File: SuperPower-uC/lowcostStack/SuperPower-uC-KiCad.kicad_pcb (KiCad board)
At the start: 4 copper layers, 92.2 x 45.2 mm, 104 parts, among them J1 Battery connector, J10 External NTC, J11 DNP, J2 Thermistor, J3 USB_B_Micro, J4 Solar in, J5 Conn_01x14_Female, J6 Conn_01x14_Female, J7 DNP, J8 regulator board, J9 MCU board, Q1 2N7002, Q2 2N7002, Q3 S8050, Q4 S8050, Q5 AO3401A, Q6 AO3401A, Q7 2N7002, Q8 2N7002, Q9 AO3401A, SW1 DNP, SW2 DNP, U1 AP9101CK6-ADTRG1, U10 FP6291LR, U11 ME6210A33P, U12 ME6210A33P, U13 ESP32-WROOM32, U14 W25Q32JVSS, U2 FS8205A, U3 LC709203FQH, U4 TP4056, U5 CH340G, U6 AMS1117-3.3, U7 PCF8563T, U8 XC6206P332MR, U9 TCA6408A, Y1 12MHZ, Y2 32.768KHz

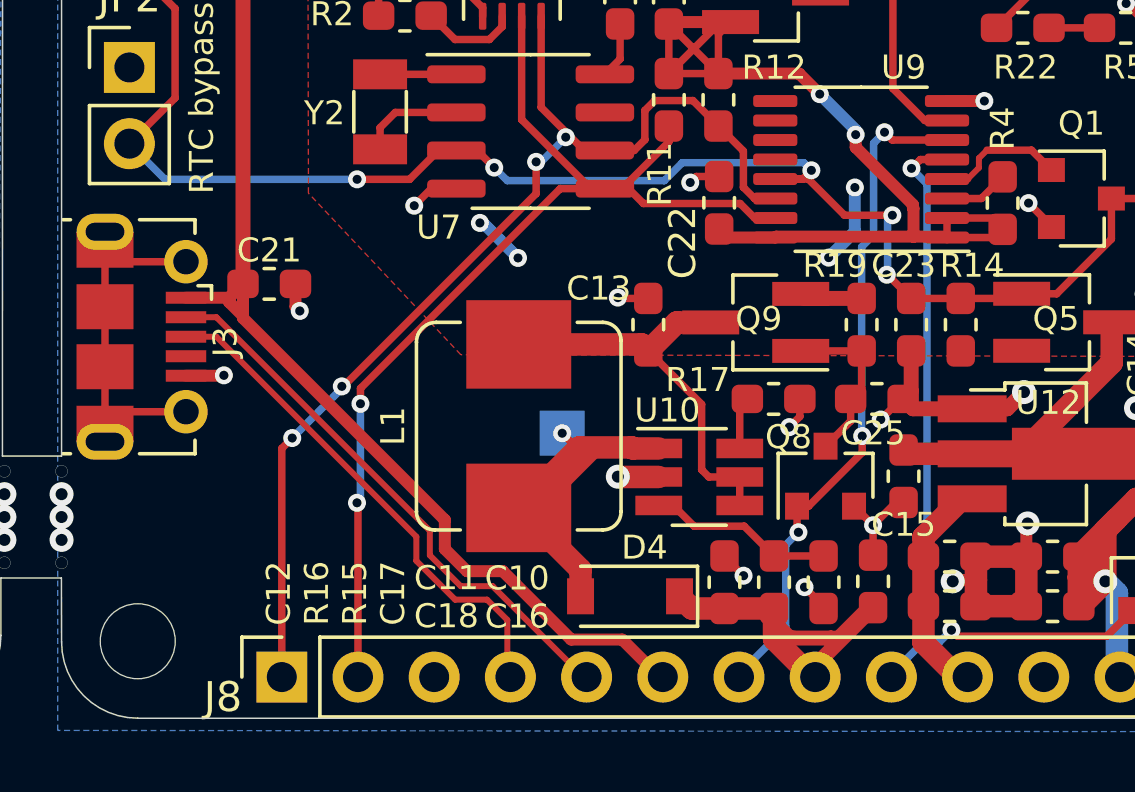
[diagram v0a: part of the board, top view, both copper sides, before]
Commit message: swapped tracks of boost conveter for planes
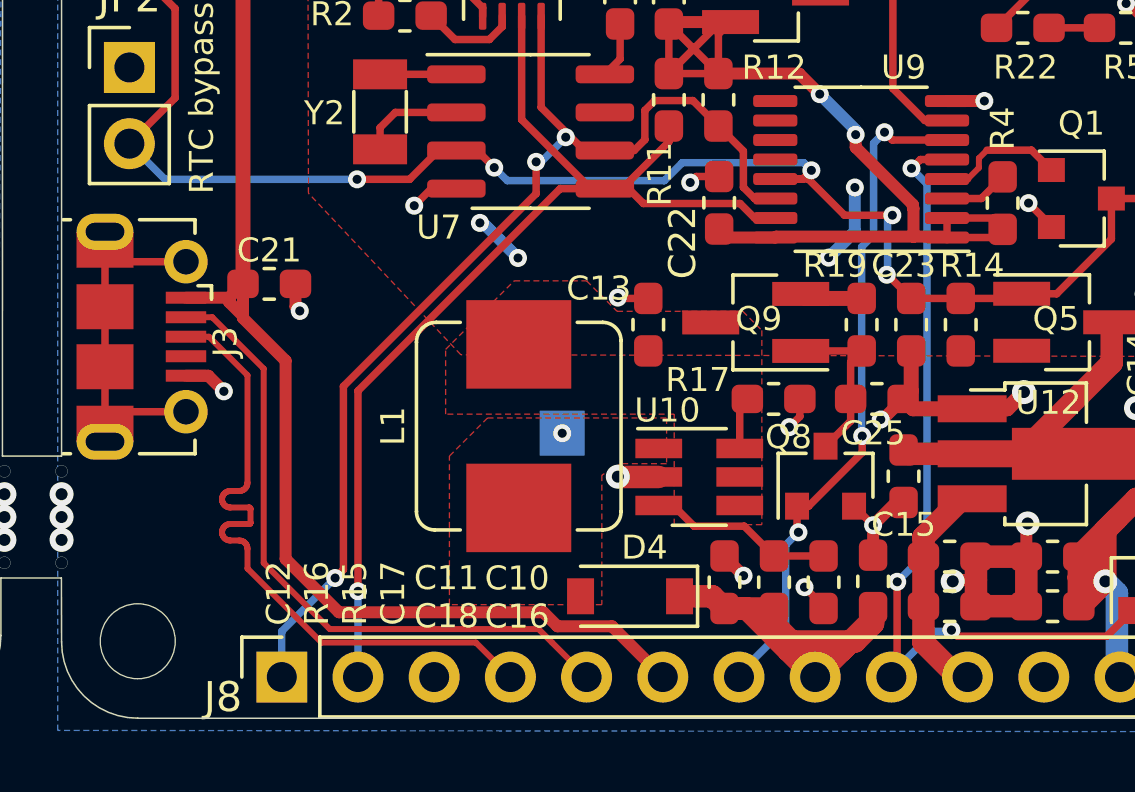
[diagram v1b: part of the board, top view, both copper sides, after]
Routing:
- net Net-(D4-Pad2): track 16.2 -> 0.61 mm
- net Net-(C13-Pad1): track 13.9 -> 0.00 mm
- net /5v: track 13.7 -> 20.8 mm
- net /D1+: track 17.0 -> 22.1 mm
- net /D1-: track 18.7 -> 22.1 mm
- net /VBUS_1: track 66.6 -> 70.0 mm
- net 3v3_EN: track 26.5 -> 28.3 mm, vias 2 -> 3
- net /SDA_1: track 37.2 -> 37.1 mm, vias 2 -> 1
- net /SCL_1: vias 4 -> 3
- added copper zone on F.Cu, net Net-(C13-Pad1)
- added copper zone on F.Cu, net Net-(D4-Pad2)

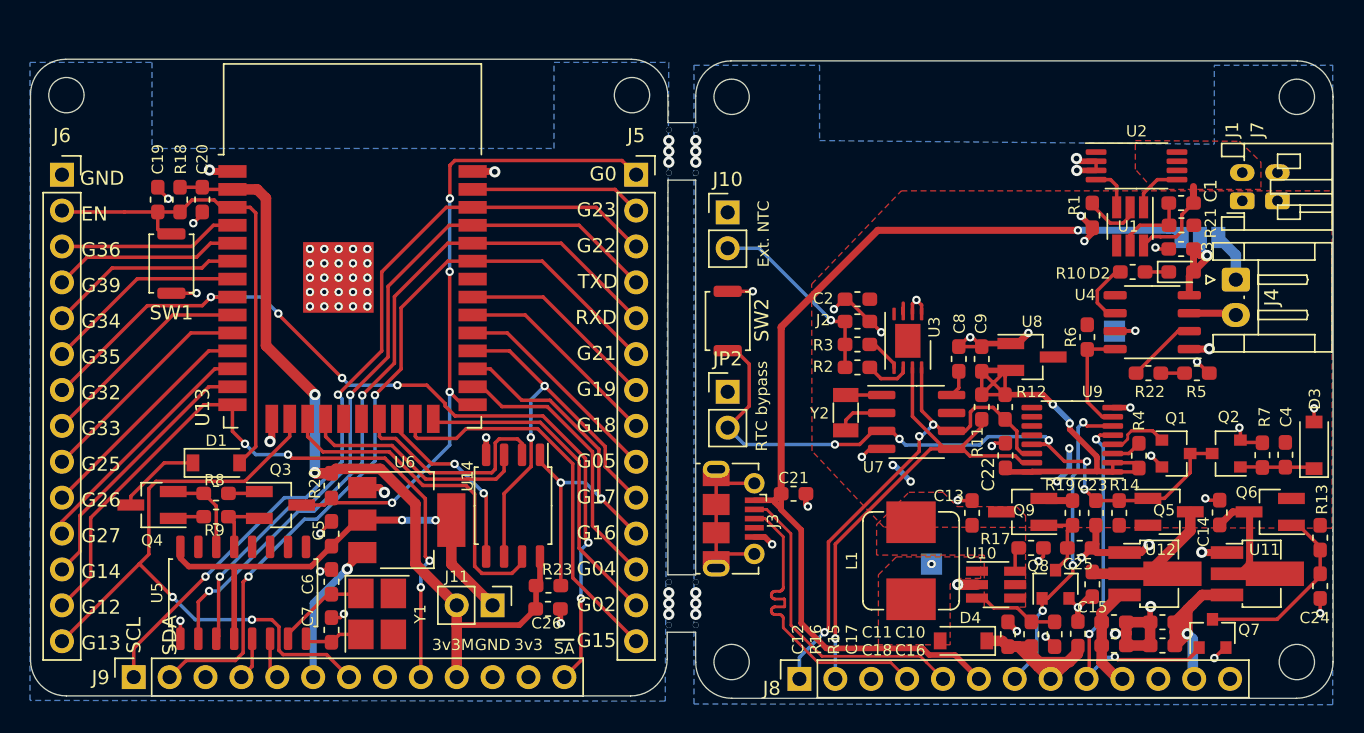
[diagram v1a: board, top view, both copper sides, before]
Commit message: modified schematic to be mostly the same to original version
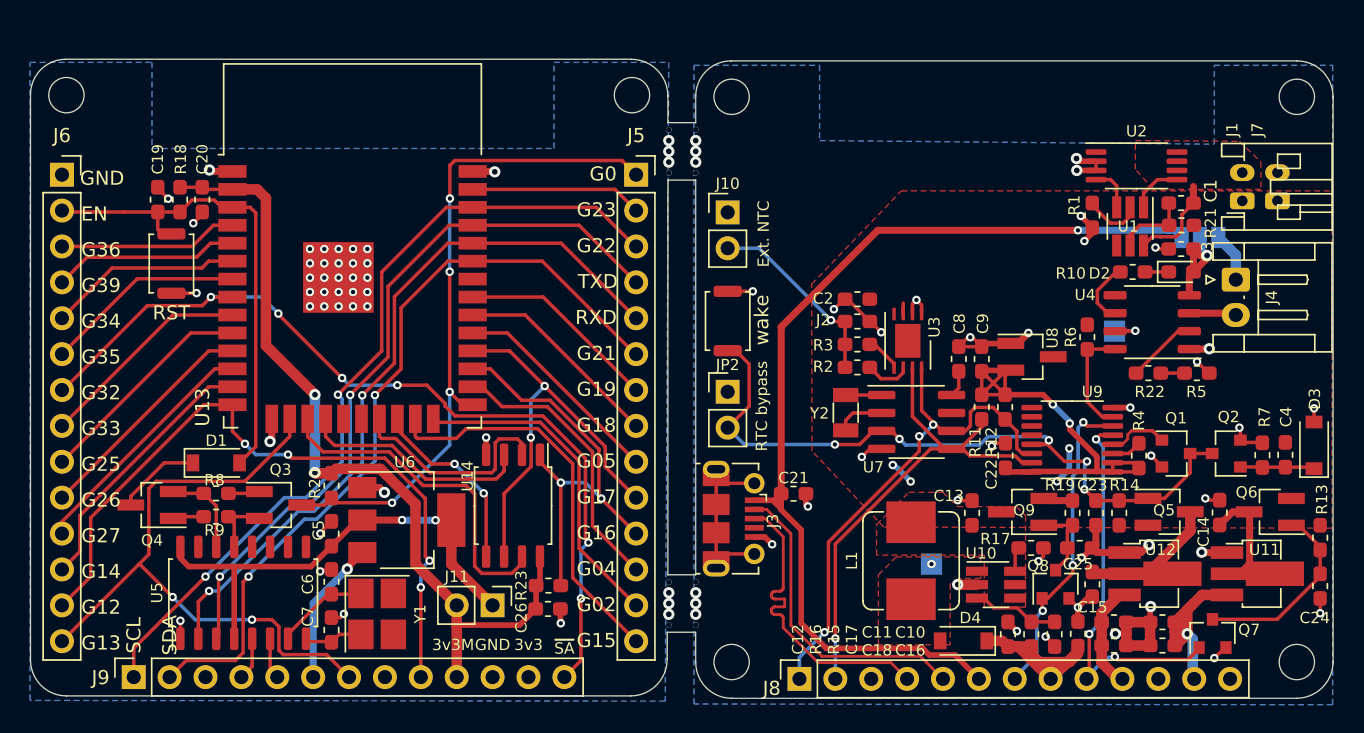
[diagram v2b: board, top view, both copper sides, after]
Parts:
- renumbered SW1 to RST, SW2 to wake
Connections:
- net /RTC and Cut-Off Module/V_I2C renamed /Charging Module/3v3_I2C
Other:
- board text added: "+"
- board text added: "-"

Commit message: changed improved and fixed a bunch of stuff
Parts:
- H1, H2, H3, H4, H5, H6: value MountingHole_Pad -> MountingHole; footprint MountingHole:MountingHole_2.5mm -> MountingHole:MountingHole_2.7mm_M2.5_Pad
- moved H2 87.1 mm to (104.2, 78.8)
- moved H4 61.8 mm to (144.2, 78.8)
- moved H5 47.1 mm to (151.3, 78.9)
- moved H6 47.1 mm to (191.3, 78.9)
- moved H1 40.0 mm to (151.3, 118.9)
- moved H3 40.0 mm to (191.3, 118.9)
- moved R5 5.26 mm to (178.9, 98.6), turned to 180 degrees
- moved R22 1.58 mm to (182.3, 98.6), turned to 180 degrees
- moved C9 0.08 mm to (169.0, 97.4)
- moved C8 0.07 mm to (167.3, 97.4)
- moved Q9 0.05 mm to (171.8, 108.3)
- renumbered RST to SW1, wake to SW2
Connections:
- C8 pad 2: /Battery Module/VBAT -> /Charging Module/3v3_I2C
- H1 pad 1: GND -> (no net)
- H2 pad 1: GND -> (no net)
- H3 pad 1: GND -> (no net)
- H4 pad 1: GND -> (no net)
- H5 pad 1: GND -> (no net)
- H6 pad 1: GND -> (no net)
- U7 pad 8: /Battery Module/VBAT -> /Charging Module/3v3_I2C
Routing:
- net /Charging Module/3v3_I2C: track 34.5 -> 22.5 mm
- net /Battery Module/VBAT: track 9.67 -> 1.23 mm, vias 4 -> 0
- net GND: track 91.9 -> 84.2 mm, vias 83 -> 73
- net Net-(C15-Pad1): track 9.60 -> 2.43 mm
- net Net-(C14-Pad1): track 7.96 -> 0.87 mm
- net Net-(R22-Pad1): track 5.00 -> 4.12 mm
- net /Charging Module/STDBY: track 4.61 -> 5.16 mm, vias 0 -> 2
- net /Charger I/O/VCHARGE: track 8.08 -> 7.53 mm
- net /VBUS_1: track 70.0 -> 69.5 mm
- net /SDA_1: track 37.1 -> 37.6 mm
- net (no net): vias 10 -> 20
- added copper zone on F.Cu, net /Charging Module/3v3_I2C
- added copper zone on F.Cu, net Net-(C14-Pad1)
- added copper zone on F.Cu, net Net-(C15-Pad1)
